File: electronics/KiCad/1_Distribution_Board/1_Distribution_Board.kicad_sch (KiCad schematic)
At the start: 10 parts, among them Q1 DMG2305UX, U1 KH-2.54FH-1X20P-H8.5, U2 KH-2.54FH-1X20P-H8.5

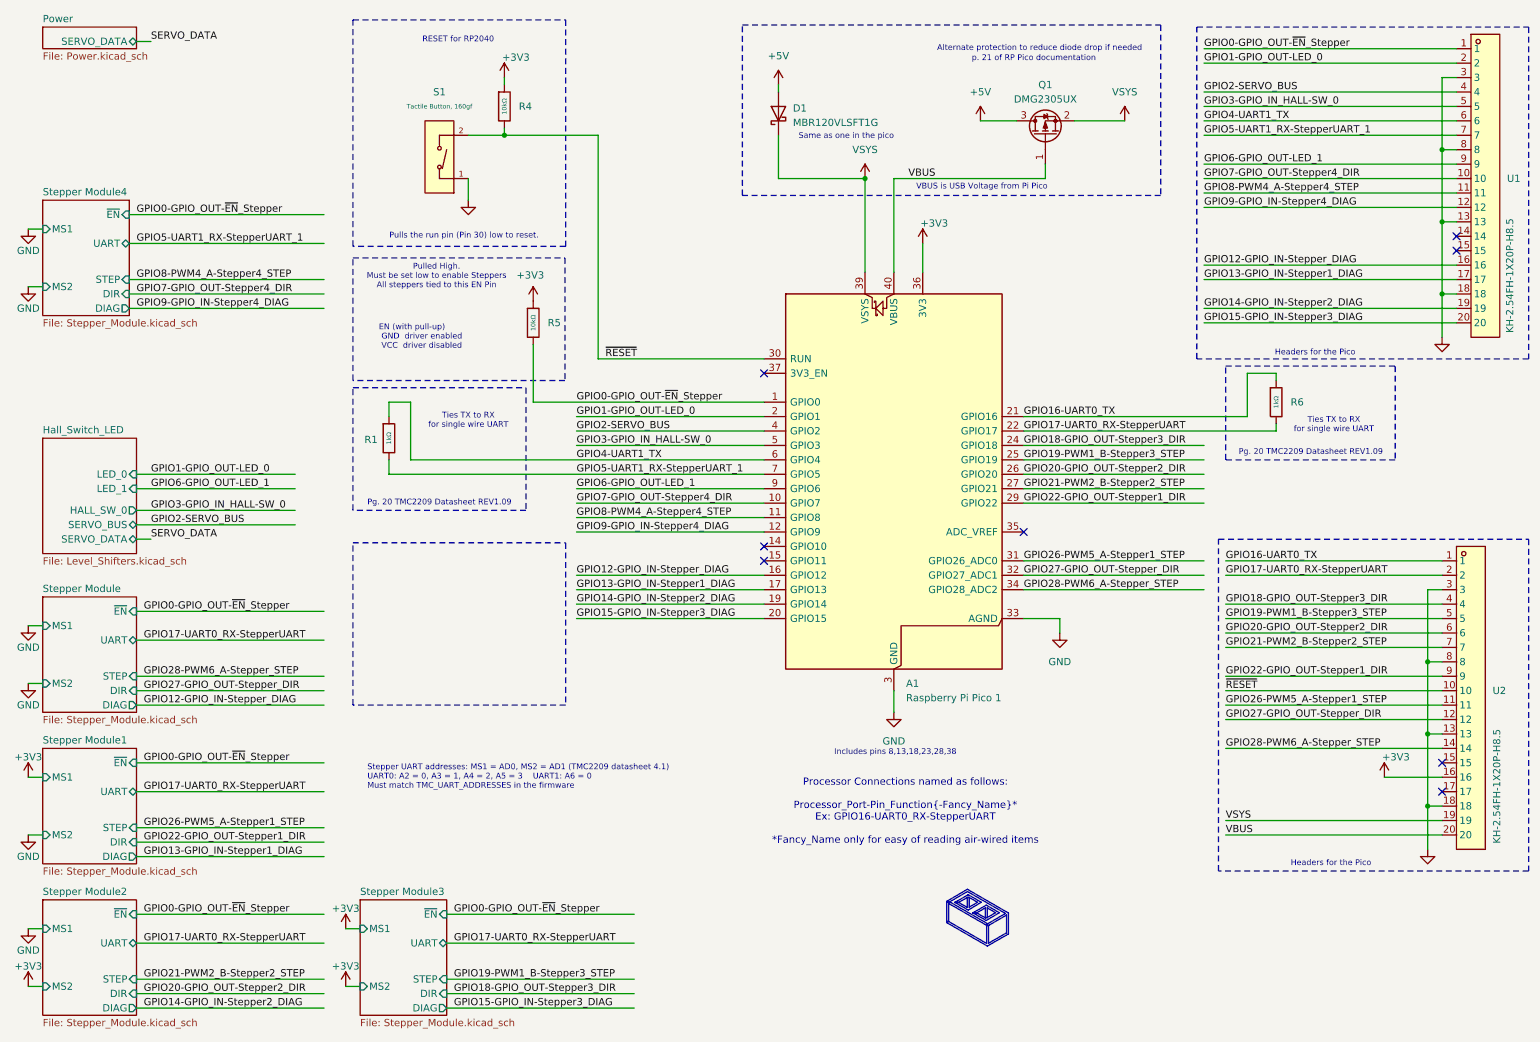
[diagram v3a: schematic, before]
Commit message: distribution board v1.5: re-layout on a 100 x 74 mm board
- outline 100 x 74 mm with the Orange Pi 5 mounting hole pattern, holes non-plated
- drivers A2 to A5 in a row along the top edge, A6 beside the Pico; every
  motor gets both a JST PH plug and a 2.54 mm header
- Pico pins reassigned so step, dir, DIAG, EN, UART0 and the two LED lines
  leave as one ordered bus under the drivers (new hwcfg needed for this rev)
- MS1/MS2 address straps through resistors: A2..A5 are 0..3 on UART0,
  A6 is 0 on UART1
- removed the 12 V and servo-voltage outputs and the second servo connector
  that carried 24 V on its power pin
- each rail runs regulator, cap, test point, indicator LED in one column
- silkscreen says what every connector is for: 24V IN, SERIAL SERVO (D, V+, G),
  LED1 to LED4, HALL, RESET, driver names and their EN corner
- GND poured on both layers and stitched; DRC clean, nothing unconnected

Co-Authored-By: Claude Opus 5.5 <noreply@anthropic.com>
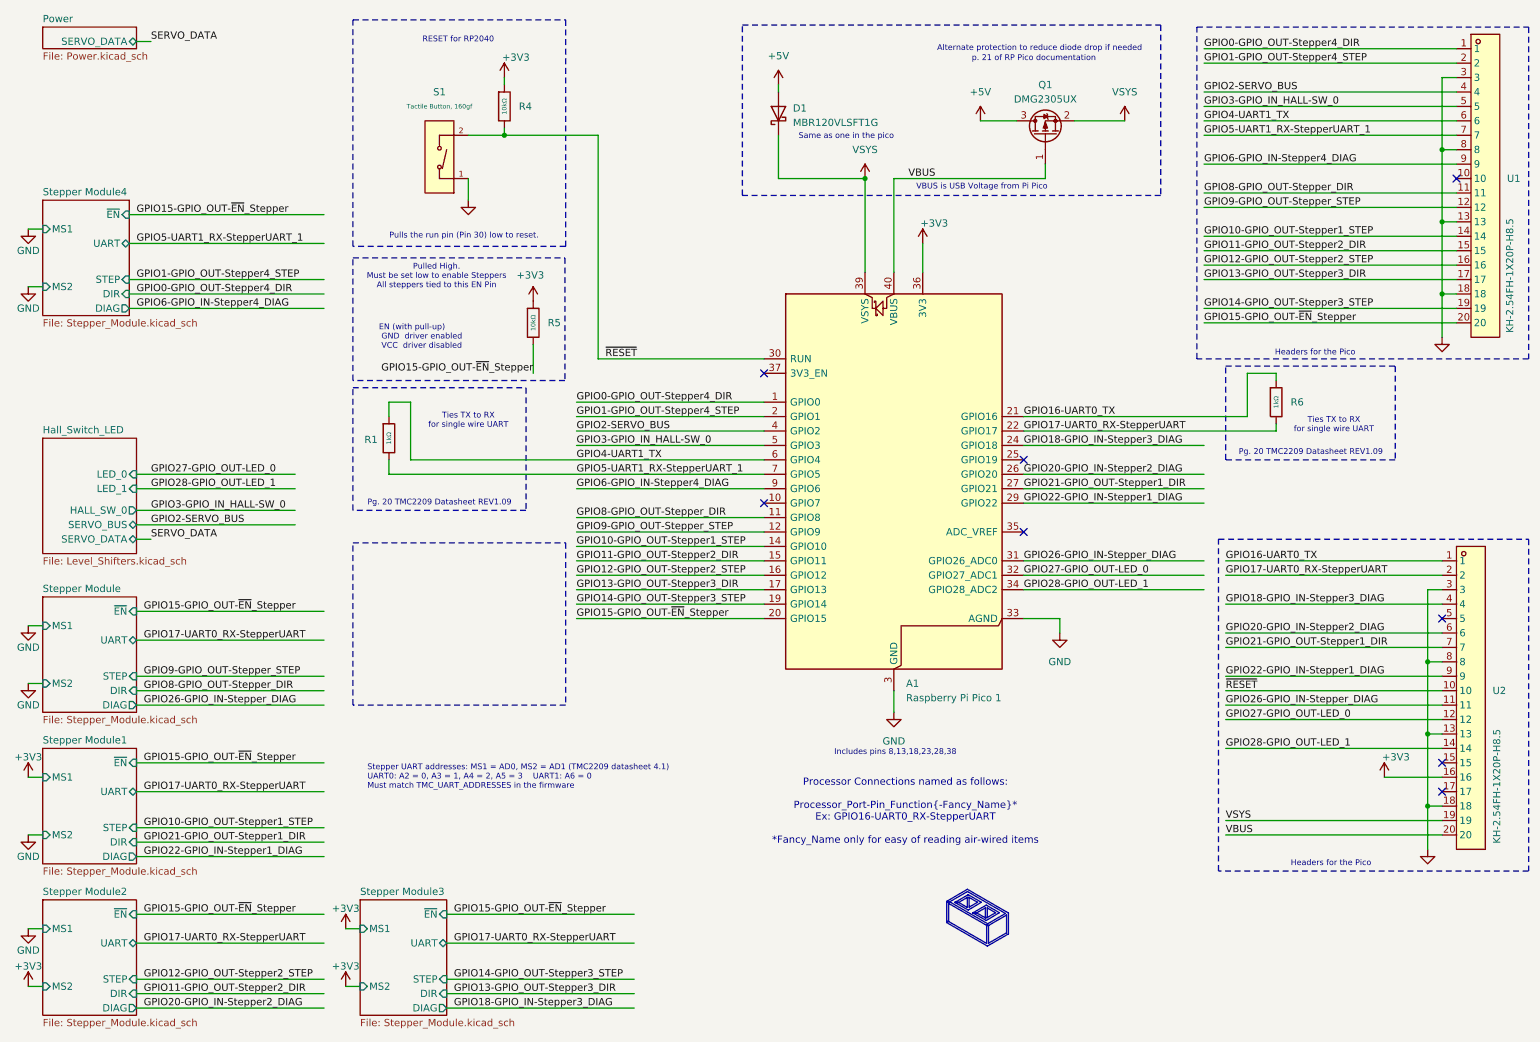
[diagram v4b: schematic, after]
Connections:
- net GPIO10-GPIO_OUT-Stepper1_STEP: now reaches U1.14
- net GPIO10-GPIO_OUT-Stepper1_STEP: now also A1.14 (GPIO10)
- net GPIO11-GPIO_OUT-Stepper2_DIR: now reaches U1.15
- net GPIO11-GPIO_OUT-Stepper2_DIR: now also A1.15 (GPIO11)
- net GPIO0-GPIO_OUT-~{EN}_Stepper renamed GPIO0-GPIO_OUT-Stepper4_DIR
- net GPIO0-GPIO_OUT-Stepper4_DIR: no longer R5.2
- net GPIO1-GPIO_OUT-LED_0 renamed GPIO1-GPIO_OUT-Stepper4_STEP
- net GPIO12-GPIO_IN-Stepper_DIAG renamed GPIO12-GPIO_OUT-Stepper2_STEP
- net GPIO13-GPIO_IN-Stepper1_DIAG renamed GPIO13-GPIO_OUT-Stepper3_DIR
- net GPIO14-GPIO_IN-Stepper2_DIAG renamed GPIO14-GPIO_OUT-Stepper3_STEP
- net GPIO15-GPIO_IN-Stepper3_DIAG renamed GPIO15-GPIO_OUT-~{EN}_Stepper
- net GPIO15-GPIO_OUT-~{EN}_Stepper: now also R5.2
- net GPIO18-GPIO_OUT-Stepper3_DIR renamed GPIO18-GPIO_IN-Stepper3_DIAG
- net GPIO19-PWM1_B-Stepper3_STEP: no longer names the net of U2.5
- net GPIO19-PWM1_B-Stepper3_STEP: no longer A1.25 (GPIO19)
- net GPIO20-GPIO_OUT-Stepper2_DIR renamed GPIO20-GPIO_IN-Stepper2_DIAG
- net GPIO21-PWM2_B-Stepper2_STEP renamed GPIO21-GPIO_OUT-Stepper1_DIR
- net GPIO22-GPIO_OUT-Stepper1_DIR renamed GPIO22-GPIO_IN-Stepper1_DIAG
- net GPIO26-PWM5_A-Stepper1_STEP renamed GPIO26-GPIO_IN-Stepper_DIAG
- net GPIO27-GPIO_OUT-Stepper_DIR renamed GPIO27-GPIO_OUT-LED_0
- net GPIO28-PWM6_A-Stepper_STEP renamed GPIO28-GPIO_OUT-LED_1
- net GPIO6-GPIO_OUT-LED_1 renamed GPIO6-GPIO_IN-Stepper4_DIAG
- net GPIO7-GPIO_OUT-Stepper4_DIR: no longer names the net of U1.10
- net GPIO7-GPIO_OUT-Stepper4_DIR: no longer A1.10 (GPIO7)
- net GPIO8-PWM4_A-Stepper4_STEP renamed GPIO8-GPIO_OUT-Stepper_DIR
- net GPIO9-GPIO_IN-Stepper4_DIAG renamed GPIO9-GPIO_OUT-Stepper_STEP

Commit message: distribution board v1.5: orange pi 5 hat link, input protection, review fixes
Mounting and the Pi link:
- The four mounting holes follow the Orange Pi 5's own pattern, 93.86 x 55.89 mm,
  taken from the vendor's STEP model.
- J41 is a 2x9 female socket under the board. It plugs onto pins 1-18 of the Pi's
  26-pin header, at the position measured from the vendor's photos against those
  holes.
- The Pi's USB/Ethernet stack is 16.2 mm tall, so the board stands on M2.5 x 20 mm
  standoffs. J41 is therefore hand-fitted, with a 15-17 mm body (DNP for assembly).
- New Pi_Link sheet. The UART crosses an ISO7721 isolator: Pi UART0_M2 on pins 8
  and 10, Pico PIO UART with GP7 TX and GP19 RX.
- Reset crosses an LTV-357T optocoupler: Pi pin 15 pulls RUN low.
- The Pi's ground stays on its side of the isolators, poured 1 mm clear of the
  board's ground.

Input:
- No fuse in the ground leg: F2 is gone.
- Q7 (AO4485 P-FET) blocks a reversed input, replacing the shunt diode D2.
- D10 (SMBJ26A) clamps surges.
- Input copper is sized for the 10 A fuse, with six vias onto the 24 V bus and
  four onto the LED lane.

Driver sockets:
- CLK (pin 6) to GND.
- PDN (pin 5) joined to UART (pin 4): modules bring PDN_UART out on either pin.

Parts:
- J1 takes the B2P-VH footprint of the part ordered, C160315.
- U3 and U4 carry the R-78K modules that are fitted.

Layout:
- 3V3 crosses above the Pico on the back.
- The reset button sits beside the Pico.
- Driver names sit between their sockets.

Co-Authored-By: Claude Opus 5.5 <noreply@anthropic.com>
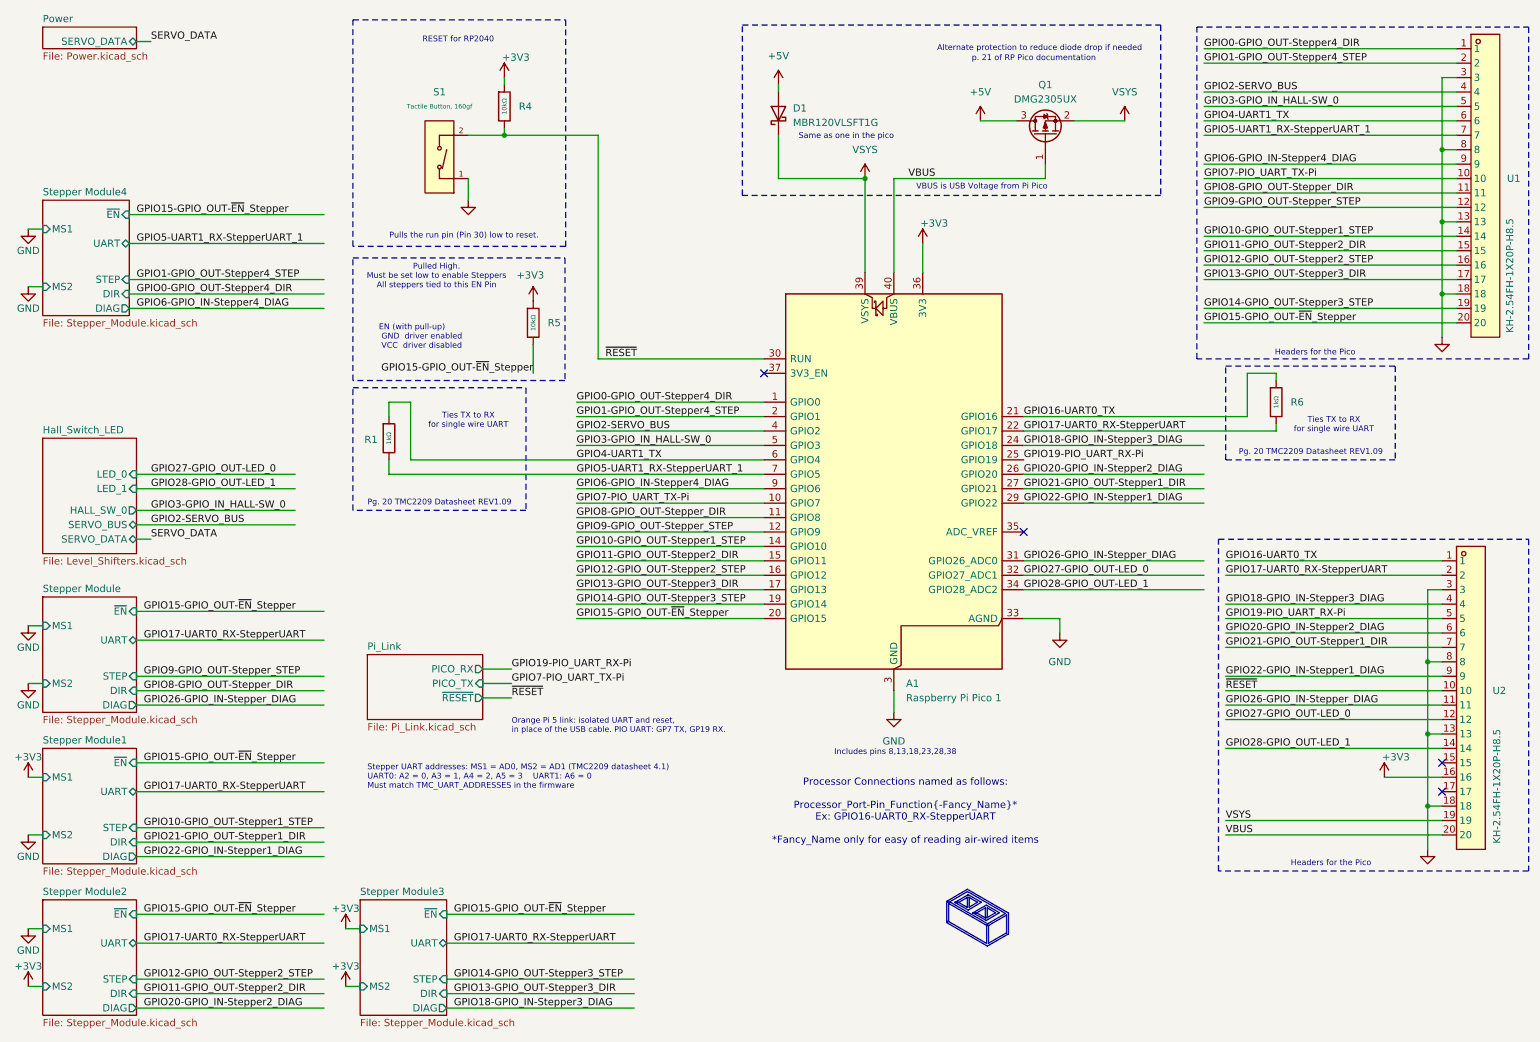
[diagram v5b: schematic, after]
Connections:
- net GPIO7-PIO_UART_TX-Pi: now reaches U1.10
- net GPIO7-PIO_UART_TX-Pi: now also A1.10 (GPIO7)
- net GPIO19-PIO_UART_RX-Pi: now reaches U2.5
- net GPIO19-PIO_UART_RX-Pi: now also A1.25 (GPIO19)
- no-connect marks 8 -> 4
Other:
- added sheet Pi_Link (Pi_Link.kicad_sch)
- note added: "Orange Pi 5 link: isolated UART and reset, in place of the USB cable. PIO UART: GP7 TX, GP19 RX."
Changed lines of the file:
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@@
 		)
 	)
-	(rectangle
-		(start 73.66 106.045)
-		(end 111.125 134.62)
-		(stroke
-			(width 0)
-			(type dash)
-		)
-		(fill
-			(type none)
-		)
-	)
 	(polyline
 		(pts
@@
 		)
 	)
-	(no_connect
-		(at 146.05 99.06)
-	)
-	(no_connect
-		(at 267.97 41.91)
-	)
 	(wire
 		(pts
@@
 		)
 	)
-	(no_connect
-		(at 191.77 91.44)
-	)
-	(no_connect
-		(at 265.43 119.38)
-	)
 	(wire
 		(pts
@@
 			)
 			(justify left bottom)
+		)
+	)
+	(sheet
+		(at 76.2 125.73)
+		(size 20.32 11.43)
+		(exclude_from_sim no)
+		(in_bom yes)
+		(on_board yes)
+		(dnp no)
+		(fields_autoplaced yes)
+		(stroke
+			(width 0.1524)
+			(type solid)
+		)
+		(fill
+			(color 0 0 0 0)
+		)
+		(property "Sheetname" "Pi_Link"
+			(at 76.2 125.0184 0)
+			(effects
+				(font
+					(size 1.27 1.27)
+				)
+				(justify left bottom)
+			)
+		)
+		(property "Sheetfile" "Pi_Link.kicad_sch"
+			(at 76.2 137.7446 0)
+			(effects
+				(font
+					(size 1.27 1.27)
+				)
+				(justify left top)
+			)
+		)
+		(pin "PICO_RX" output
+			(at 96.52000000000001 128.27 0)
+			(effects
+				(font
+					(size 1.27 1.27)
+				)
+				(justify right)
+			)
+		)
+		(pin "PICO_TX" input
+			(at 96.52000000000001 130.81 0)
+			(effects
+				(font
+					(size 1.27 1.27)
+				)
+				(justify right)
+			)
+		)
+		(pin "~{RESET}" output
+			(at 96.52000000000001 133.35 0)
+			(effects
+				(font
+					(size 1.27 1.27)
+				)
+				(justify right)
+			)
+		)
+		(instances
+			(project "1_Distribution_Board"
+				(path "/d53c8c01-e754-4310-8a73-7d7c95e64cd3"
+					(page "9")
+				)
+			)
+		)
+	)
+	(wire
+		(pts
+			(xy 96.52000000000001 128.27) (xy 101.6 128.27)
+		)
+		(stroke
+			(width 0)
+			(type default)
+		)
+	)
+	(label "GPIO19-PIO_UART_RX-Pi"
+		(at 101.6 128.27 0)
+		(effects
+			(font
+				(size 1.27 1.27)
+			)
+			(justify left bottom)
+		)
+	)
+	(wire
+		(pts
+			(xy 96.52000000000001 130.81) (xy 101.6 130.81)
+		)
+		(stroke
+			(width 0)
+			(type default)
+		)
+	)
+	(label "GPIO7-PIO_UART_TX-Pi"
+		(at 101.6 130.81 0)
+		(effects
+			(font
+				(size 1.27 1.27)
+			)
+			(justify left bottom)
+		)
+	)
+	(wire
+		(pts
+			(xy 96.52000000000001 133.35) (xy 101.6 133.35)
+		)
+		(stroke
+			(width 0)
+			(type default)
+		)
+	)
+	(label "~{RESET}"
+		(at 101.6 133.35 0)
+		(effects
+			(font
+				(size 1.27 1.27)
+			)
+			(justify left bottom)
+		)
+	)
+	(wire
+		(pts
+			(xy 113.03 99.06) (xy 146.05 99.06)
+		)
+		(stroke
+			(width 0)
+			(type default)
+		)
+	)
+	(label "GPIO7-PIO_UART_TX-Pi"
+		(at 113.03 99.06 0)
+		(effects
+			(font
+				(size 1.27 1.27)
+			)
+			(justify left bottom)
+		)
+	)
+	(label "GPIO19-PIO_UART_RX-Pi"
+		(at 191.77 91.44 0)
+		(effects
+			(font
+				(size 1.27 1.27)
+			)
+			(justify left bottom)
+		)
+	)
+	(wire
+		(pts
+			(xy 223.52 41.91) (xy 267.97 41.91)
+		)
+		(stroke
+			(width 0)
+			(type default)
+		)
+	)
+	(label "GPIO7-PIO_UART_TX-Pi"
+		(at 223.52 41.91 0)
+		(effects
+			(font
+				(size 1.27 1.27)
+			)
+			(justify left bottom)
+		)
+	)
+	(wire
+		(pts
+			(xy 227.33 119.38) (xy 265.43 119.38)
+		)
+		(stroke
+			(width 0)
+			(type default)
+		)
+	)
+	(label "GPIO19-PIO_UART_RX-Pi"
+		(at 227.33 119.38 0)
+		(effects
+			(font
+				(size 1.27 1.27)
+			)
+			(justify left bottom)
+		)
+	)
+	(text "Orange Pi 5 link: isolated UART and reset,\nin place of the USB cable. PIO UART: GP7 TX, GP19 RX."
+		(exclude_from_sim no)
+		(at 101.6 139.7 0)
+		(effects
+			(font
+				(size 1.0 1.0)
+			)
+			(justify left bottom)

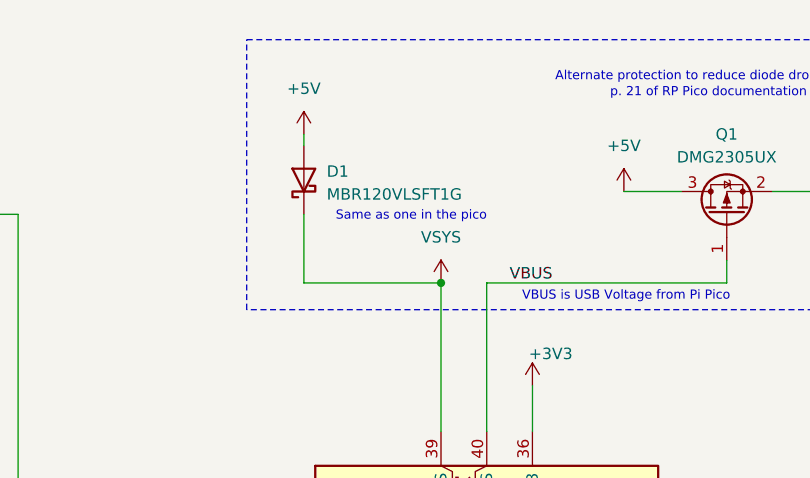
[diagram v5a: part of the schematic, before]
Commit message: distribution board v1.5: D1 is an MBR120LSFT1G (in stock at JLCPCB)
The assembler ran short of D1's part, onsemi's MBR120VLSFT1G (LCSC C223608).
D1 is the Schottky from the 5 V regulator to the Pico's VSYS, beside Q1, so
it carries about 0.1 A only while USB powers the Pico, and sees at most 5 V
in reverse. onsemi's MBR120LSFT1G (C891416) is the same family and SOD-123FL
package, 1 A and 20 V, with the cathode on pin 1 like the part it replaces;
its footprint at the assembler lands on D1's pads cathode on cathode.

Only D1's value and LCSC fields change, in the schematic and on the board.
The position file, IPC-D-356 netlist and Gerbers are unchanged; the BOM
changes in D1's line. DRC, schematic parity and ERC are as before.

Co-Authored-By: Claude Opus 5.5 <noreply@anthropic.com>
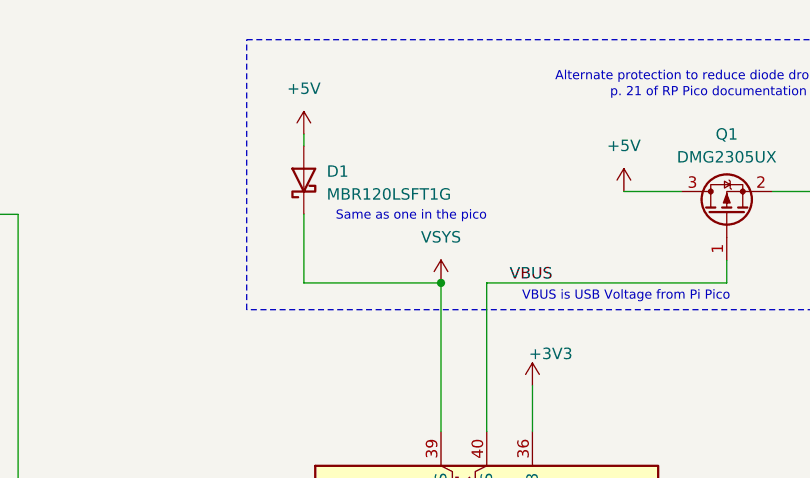
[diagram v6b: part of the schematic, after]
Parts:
- D1: value MBR120VLSFT1G -> MBR120LSFT1G; LCSC C223608 -> C891416
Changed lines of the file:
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@@
 			)
 		)
-		(property "Value" "MBR120VLSFT1G"
+		(property "Value" "MBR120LSFT1G"
 			(at 151.13 32.0674 90)
 			(show_name no)
@@
 			)
 		)
-		(property "LCSC" "C223608"
+		(property "LCSC" "C891416"
 			(at 148.59 30.48 0)
 			(hide yes)
